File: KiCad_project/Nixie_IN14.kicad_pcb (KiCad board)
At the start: 2 copper layers, 148.3 x 69.3 mm, 65 parts, among them J1 Conn_01x10_Pin, J2 Conn_01x07_Pin, J3 Conn_01x07_Pin, J4 Conn_01x10_Pin, J5 Conn_01x07_Pin, J6 Conn_01x07_Pin, J7 USB_C_Receptacle_PowerOnly_6P, Q1 IRF540N, Q2 MMBTA42, U1 BME280_module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

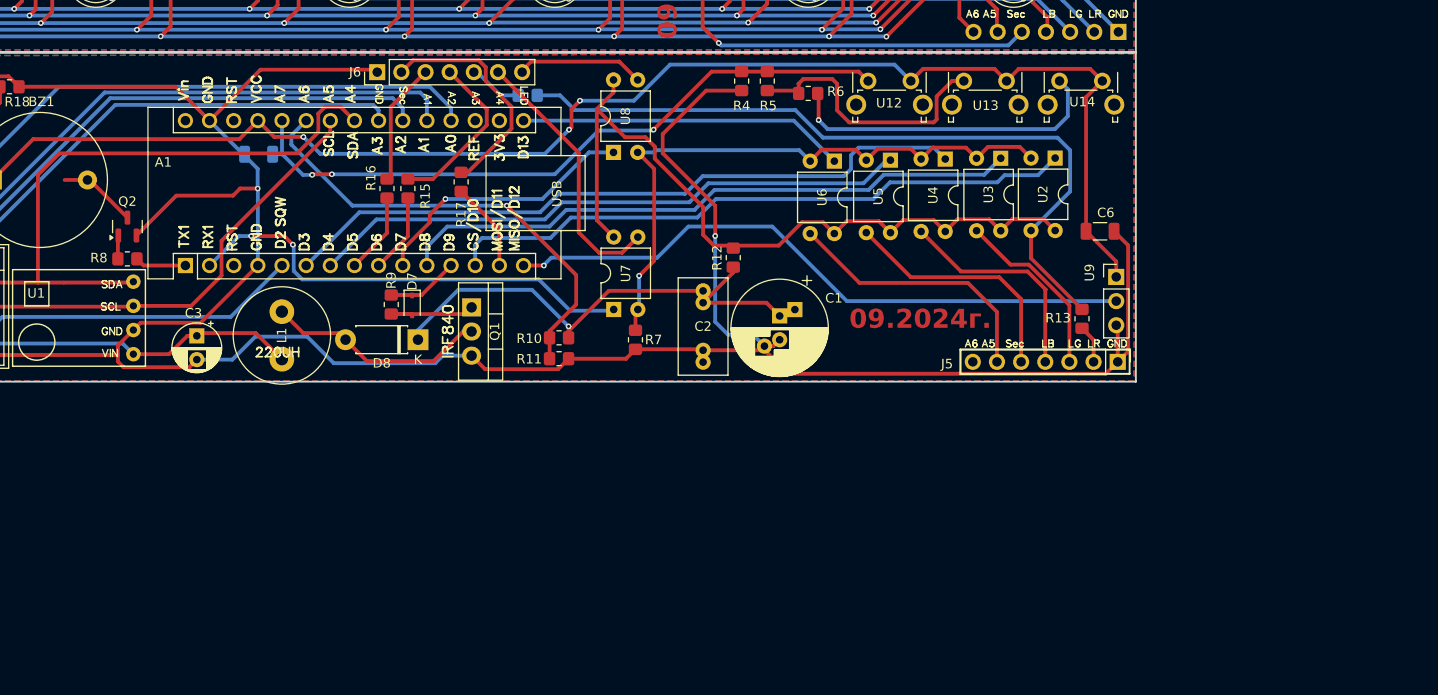
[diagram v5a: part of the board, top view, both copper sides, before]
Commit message: placed transistors instead of optic pairs
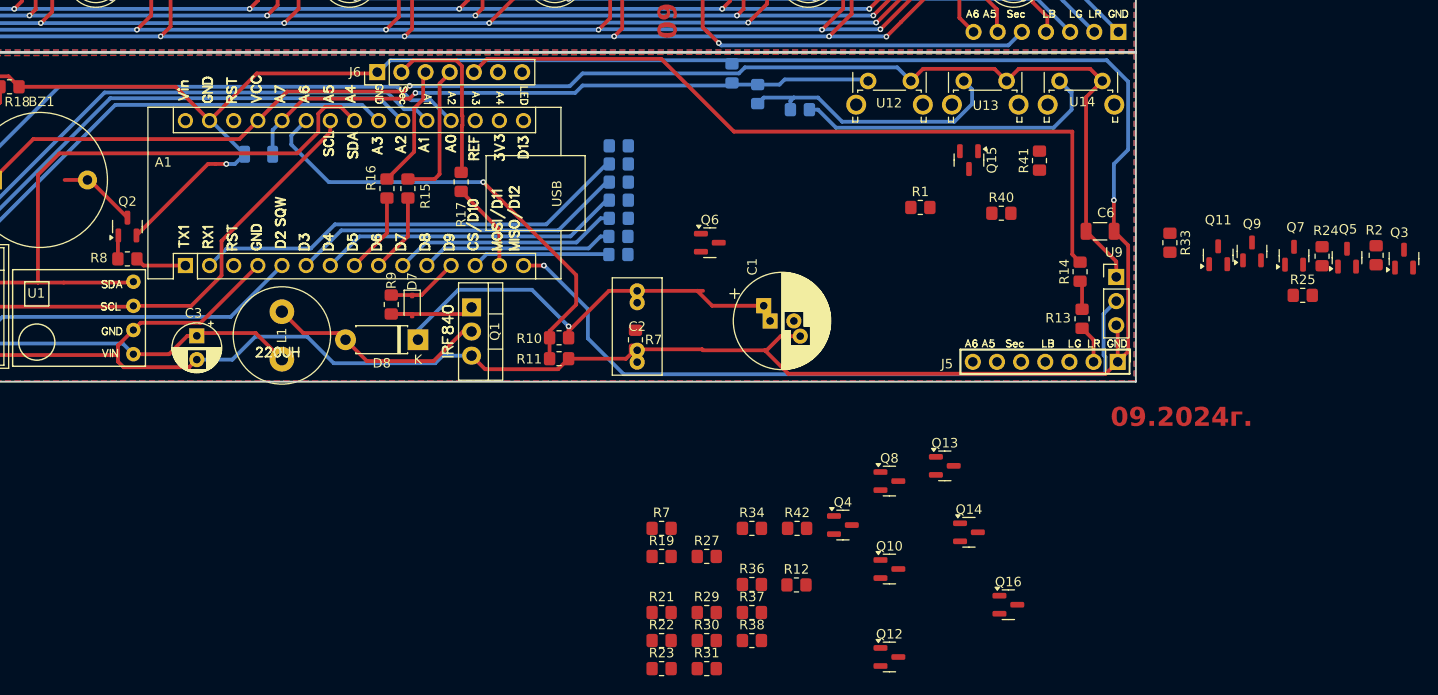
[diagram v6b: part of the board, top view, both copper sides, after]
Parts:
- removed U2, U3, U4, U5, U6, U7, U8: TLP627, Package_DIP:DIP-4_W7.62mm
- added Q10: MMBTA42, Package_TO_SOT_SMD:SOT-23, F.Cu at (188.5, 144.2)
- added Q11: MMBTA92, Package_TO_SOT_SMD:SOT-23, F.Cu at (223.1, 111.2)
- added Q12: MMBTA42, Package_TO_SOT_SMD:SOT-23, F.Cu at (188.5, 153.4)
- added Q13: MMBTA92, Package_TO_SOT_SMD:SOT-23, F.Cu at (194.3, 133.3)
- added Q14: MMBTA42, Package_TO_SOT_SMD:SOT-23, F.Cu at (196.8, 140.3)
- added Q15: MMBTA92, Package_TO_SOT_SMD:SOT-23, F.Cu at (196.8, 101.2)
- added Q16: MMBTA42, Package_TO_SOT_SMD:SOT-23, F.Cu at (201.0, 148.0)
- added Q3: MMBTA92, Package_TO_SOT_SMD:SOT-23, F.Cu at (242.6, 111.6)
- added Q4: MMBTA42, Package_TO_SOT_SMD:SOT-23, F.Cu at (183.6, 139.6)
- added Q5: MMBTA92, Package_TO_SOT_SMD:SOT-23, F.Cu at (236.6, 111.5)
- added Q6: MMBTA42, Package_TO_SOT_SMD:SOT-23, F.Cu at (169.6, 109.9)
- added Q7: MMBTA92, Package_TO_SOT_SMD:SOT-23, F.Cu at (231.0, 111.3)
- added Q8: MMBTA42, Package_TO_SOT_SMD:SOT-23, F.Cu at (188.5, 134.9)
- added Q9: MMBTA92, Package_TO_SOT_SMD:SOT-23, F.Cu at (226.6, 110.8)
- added R1: 20k, Resistor_SMD:R_0805_2012Metric_Pad1.20x1.40mm_HandSolder, F.Cu at (191.7, 106.2)
- added R19: 1M, Resistor_SMD:R_0805_2012Metric_Pad1.20x1.40mm_HandSolder, F.Cu at (164.5, 142.9)
- added R2: 10k, Resistor_SMD:R_0805_2012Metric_Pad1.20x1.40mm_HandSolder, F.Cu at (239.7, 111.2)
- added R20: 10k, Resistor_SMD:R_0805_2012Metric_Pad1.20x1.40mm_HandSolder, B.Cu at (160.0, 111.1)
- added R21: 20k, Resistor_SMD:R_0805_2012Metric_Pad1.20x1.40mm_HandSolder, F.Cu at (164.5, 148.8)
- added R22: 10k, Resistor_SMD:R_0805_2012Metric_Pad1.20x1.40mm_HandSolder, F.Cu at (164.5, 151.7)
- added R23: 20k, Resistor_SMD:R_0805_2012Metric_Pad1.20x1.40mm_HandSolder, F.Cu at (164.5, 154.7)
- added R24: 10k, Resistor_SMD:R_0805_2012Metric_Pad1.20x1.40mm_HandSolder, F.Cu at (234.0, 111.3)
- added R25: 1M, Resistor_SMD:R_0805_2012Metric_Pad1.20x1.40mm_HandSolder, F.Cu at (232.0, 115.4)
- added R26: 10k, Resistor_SMD:R_0805_2012Metric_Pad1.20x1.40mm_HandSolder, B.Cu at (160.0, 109.2)
- added R27: 1M, Resistor_SMD:R_0805_2012Metric_Pad1.20x1.40mm_HandSolder, F.Cu at (169.3, 142.9)
- added R28: 10k, Resistor_SMD:R_0805_2012Metric_Pad1.20x1.40mm_HandSolder, B.Cu at (160.0, 103.5)
- added R29: 20k, Resistor_SMD:R_0805_2012Metric_Pad1.20x1.40mm_HandSolder, F.Cu at (169.3, 148.8)
- added R30: 10k, Resistor_SMD:R_0805_2012Metric_Pad1.20x1.40mm_HandSolder, F.Cu at (169.3, 151.7)
- added R31: 1M, Resistor_SMD:R_0805_2012Metric_Pad1.20x1.40mm_HandSolder, F.Cu at (169.3, 154.7)
- added R32: 10k, Resistor_SMD:R_0805_2012Metric_Pad1.20x1.40mm_HandSolder, B.Cu at (160.0, 105.4)
- added R33: 10k, Resistor_SMD:R_0805_2012Metric_Pad1.20x1.40mm_HandSolder, F.Cu at (218.0, 109.9)
- added R34: 1M, Resistor_SMD:R_0805_2012Metric_Pad1.20x1.40mm_HandSolder, F.Cu at (174.0, 139.9)
- added R35: 10k, Resistor_SMD:R_0805_2012Metric_Pad1.20x1.40mm_HandSolder, B.Cu at (160.0, 99.7)
- added R36: 20k, Resistor_SMD:R_0805_2012Metric_Pad1.20x1.40mm_HandSolder, F.Cu at (174.0, 145.8)
- added R37: 10k, Resistor_SMD:R_0805_2012Metric_Pad1.20x1.40mm_HandSolder, F.Cu at (174.0, 148.8)
- added R38: 1M, Resistor_SMD:R_0805_2012Metric_Pad1.20x1.40mm_HandSolder, F.Cu at (174.0, 151.7)
- added R39: 10k, Resistor_SMD:R_0805_2012Metric_Pad1.20x1.40mm_HandSolder, B.Cu at (160.0, 101.6)
- added R40: 20k, Resistor_SMD:R_0805_2012Metric_Pad1.20x1.40mm_HandSolder, F.Cu at (200.3, 106.8)
- added R41: 10k, Resistor_SMD:R_0805_2012Metric_Pad1.20x1.40mm_HandSolder, F.Cu at (204.3, 101.2)
- added R42: 1M, Resistor_SMD:R_0805_2012Metric_Pad1.20x1.40mm_HandSolder, F.Cu at (178.8, 139.9)
- added R43: 10k, Resistor_SMD:R_0805_2012Metric_Pad1.20x1.40mm_HandSolder, B.Cu at (160.0, 107.3)
- added R7: 20k, Resistor_SMD:R_0805_2012Metric_Pad1.20x1.40mm_HandSolder, F.Cu at (164.5, 139.9)
- R14: moved to F.Cu
- R4, R5, R6: moved to B.Cu
- moved R14 61.0 mm to (208.5, 112.9), turned to 90 degrees
- moved R12 35.1 mm to (178.7, 145.9), turned to 0 degrees
- moved C2 6.93 mm to (162.0, 114.9)
- moved R6 1.91 mm to (179.1, 95.9)
- moved R5 1.70 mm to (174.6, 94.2)
- moved R4 1.30 mm to (171.9, 92.1), turned to 90 degrees
- moved C1 1.13 mm to (175.9, 118.1), turned to 0 degrees
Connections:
- J5 pad 2: SEC_1 -> LED_R
- J5 pad 3: A1 -> LED_G
- J5 pad 4: A2 -> LED_B
- J5 pad 5: A3 -> SEC_2
- J5 pad 6: A4 -> A5
- J5 pad 7: LED_B_NCC -> A6
- J6 pad 2: LED_R -> SEC_1
- J6 pad 3: LED_G -> A1
- J6 pad 4: LED_B -> A2
- J6 pad 5: SEC_2 -> A3
- J6 pad 6: A5 -> A4
- J6 pad 7: A6 -> LED_B_NCC
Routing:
- net HIGH_VOLTAGE: track 80.2 -> 0.00 mm
- net Net-(Q3-E): track 79.1 -> 3.04 mm
- net SEC_2: track 5.68 -> 80.8 mm
- net Net-(R7-Pad1): track 66.0 -> 0.00 mm, vias 1 -> 0
- net SEC_CONTROL: track 67.0 -> 14.6 mm
- net GNDREF: track 343.0 -> 391.5 mm
- net A1_CONTROL: track 66.2 -> 20.4 mm
- net A2_CONTROL: track 73.7 -> 35.5 mm
- net A4_CONTROL: track 34.5 -> 0.00 mm
- net A3_CONTROL: track 63.5 -> 32.2 mm
- net A4: track 28.3 -> 0.00 mm
- net A5: track 28.2 -> 0.00 mm
- net A3: track 26.5 -> 0.00 mm
- net A2: track 23.3 -> 0.00 mm
- net A1: track 19.0 -> 0.00 mm
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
